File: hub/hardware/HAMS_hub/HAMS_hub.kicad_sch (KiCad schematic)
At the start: 32 parts, among them J1 Conn_02x07_Odd_Even, J10 Conn_01x04, J2 Conn_02x07_Odd_Even, J3 Conn_01x02, J4 Conn_01x04, J5 Conn_01x04, J6 Conn_01x07, J7 Conn_01x04, J8 Conn_01x04, J9 Conn_01x04, Q1 DMG3406L, U1 TCA9406DC, U2 NCP5501, U3 NRF24L01_Breakout

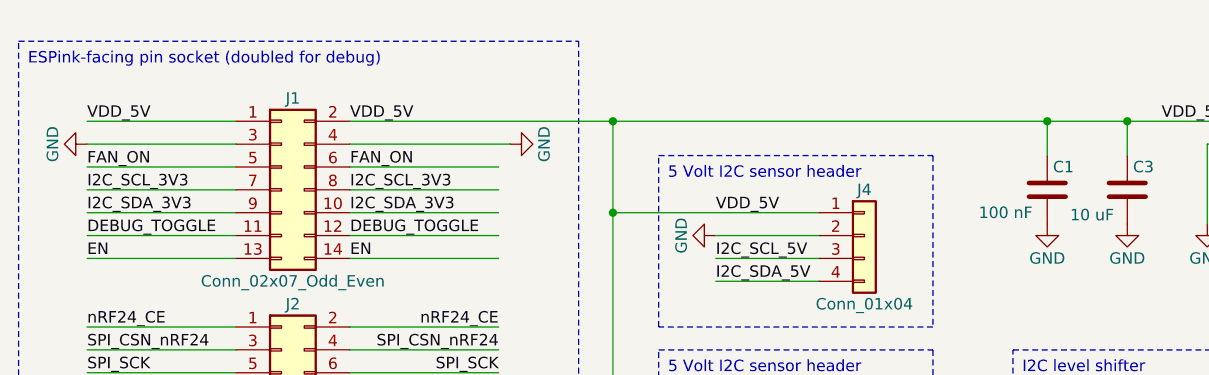
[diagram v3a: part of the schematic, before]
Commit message: Improve HAMS node & hub HW: PCB update
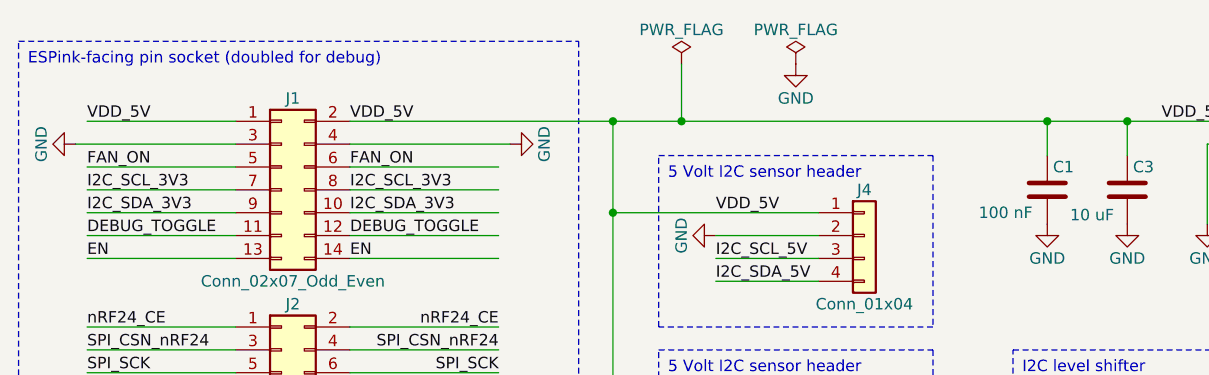
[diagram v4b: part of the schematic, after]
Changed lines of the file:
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@@
 	)
 	(junction
+		(at 90.17 25.4)
+		(diameter 0)
+		(color 0 0 0 0)
+	)
+	(junction
 		(at 233.68 118.11)
 		(diameter 0)
@@
 	(wire
 		(pts
-			(xy 82.55 25.4) (xy 130.81 25.4)
+			(xy 82.55 25.4) (xy 90.17 25.4)
 		)
 		(stroke
@@
 	(wire
 		(pts
-			(xy 24.13 27.94) (xy 40.64 27.94)
+			(xy 22.86 27.94) (xy 40.64 27.94)
 		)
 		(stroke
@@
 	(wire
 		(pts
+			(xy 90.17 25.4) (xy 130.81 25.4)
+		)
+		(stroke
+			(width 0)
+			(type default)
+		)
+	)
+	(wire
+		(pts
 			(xy 93.98 38.1) (xy 105.41 38.1)
 		)
@@
 	(wire
 		(pts
+			(xy 90.17 19.05) (xy 90.17 25.4)
+		)
+		(stroke
+			(width 0)
+			(type default)
+		)
+	)
+	(wire
+		(pts
 			(xy 24.13 48.26) (xy 40.64 48.26)
 		)
@@
 	)
 	(symbol
+		(lib_id "power:PWR_FLAG")
+		(at 102.87 19.05 0)
+		(unit 1)
+		(exclude_from_sim no)
+		(in_bom yes)
+		(on_board yes)
+		(dnp no)
+		(property "Reference" "#FLG02"
+			(at 102.87 17.145 0)
+			(effects
+				(font
+					(size 1.27 1.27)
+				)
+				(hide yes)
+			)
+		)
+		(property "Value" "PWR_FLAG"
+			(at 102.87 15.24 0)
+			(effects
+				(font
+					(size 1.27 1.27)
+				)
+			)
+		)
+		(property "Footprint" ""
+			(at 102.87 19.05 0)
+			(effects
+				(font
+					(size 1.27 1.27)
+				)
+				(hide yes)
+			)
+		)
+		(property "Datasheet" "~"
+			(at 102.87 19.05 0)
+			(effects
+				(font
+					(size 1.27 1.27)
+				)
+				(hide yes)
+			)
+		)
+		(property "Description" "Special symbol for telling ERC where power comes from"
+			(at 102.87 19.05 0)
+			(effects
+				(font
+					(size 1.27 1.27)
+				)
+				(hide yes)
+			)
+		)
+		(pin "1"
+		)
+		(instances
+			(project "HAMS_hub"
+				(path "/fa0fd52b-f5da-4d11-b769-e40ce6054164"
+					(reference "#FLG02")
+					(unit 1)
+				)
+			)
+		)
+	)
+	(symbol
 		(lib_id "power:GND")
 		(at 175.26 146.05 0)
@@
 	(symbol
 		(lib_id "power:GND")
-		(at 24.13 27.94 270)
+		(at 22.86 27.94 270)
 		(unit 1)
 		(exclude_from_sim no)
@@
 		(dnp no)
 		(property "Reference" "#PWR01"
-			(at 17.78 27.94 0)
+			(at 16.51 27.94 0)
 			(effects
 				(font
@@
 		)
 		(property "Value" "GND"
-			(at 20.32 27.94 0)
+			(at 19.05 27.94 0)
 			(effects
 				(font
@@
 		)
 		(property "Footprint" ""
-			(at 24.13 27.94 0)
+			(at 22.86 27.94 0)
 			(effects
 				(font
@@
 		)
 		(property "Datasheet" ""
-			(at 24.13 27.94 0)
+			(at 22.86 27.94 0)
 			(effects
 				(font
@@
 		)
 		(property "Description" "Power symbol creates a global label with name \"GND\" , ground"
-			(at 24.13 27.94 0)
+			(at 22.86 27.94 0)
 			(effects
 				(font
@@
 	(symbol
 		(lib_id "power:GND")
+		(at 102.87 19.05 0)
+		(unit 1)
+		(exclude_from_sim no)
+		(in_bom yes)
+		(on_board yes)
+		(dnp no)
+		(property "Reference" "#PWR029"
+			(at 102.87 25.4 0)
+			(effects
+				(font
+					(size 1.27 1.27)
+				)
+				(hide yes)
+			)
+		)
+		(property "Value" "GND"
+			(at 102.87 22.86 0)
+			(effects
+				(font
+					(size 1.27 1.27)
+				)
+			)
+		)
+		(property "Footprint" ""
+			(at 102.87 19.05 0)
+			(effects
+				(font
+					(size 1.27 1.27)
+				)
+				(hide yes)
+			)
+		)
+		(property "Datasheet" ""
+			(at 102.87 19.05 0)
+			(effects
+				(font
+					(size 1.27 1.27)
+				)
+				(hide yes)
+			)
+		)
+		(property "Description" "Power symbol creates a global label with name \"GND\" , ground"
+			(at 102.87 19.05 0)
+			(effects
+				(font
+					(size 1.27 1.27)
+				)
+				(hide yes)
+			)
+		)
+		(pin "1"
+		)
+		(instances
+			(project "HAMS_hub"
+				(path "/fa0fd52b-f5da-4d11-b769-e40ce6054164"
+					(reference "#PWR029")
+					(unit 1)
+				)
+			)
+		)
+	)
+	(symbol
+		(lib_id "power:GND")
 		(at 24.13 63.5 270)
 		(unit 1)
@@
 					(unit 1)
 				)
+			)
+		)
+	)
+	(symbol
+		(lib_id "power:PWR_FLAG")
+		(at 90.17 19.05 0)
+		(unit 1)
+		(exclude_from_sim no)
+		(in_bom yes)
+		(on_board yes)
+		(dnp no)
+		(property "Reference" "#FLG01"
+			(at 90.17 17.145 0)
+			(effects
+				(font
+					(size 1.27 1.27)
+				)
+				(hide yes)
+			)
+		)
+		(property "Value" "PWR_FLAG"
+			(at 90.17 15.24 0)
+			(effects
+				(font
+					(size 1.27 1.27)
+				)
+			)
+		)
+		(property "Footprint" ""
+			(at 90.17 19.05 0)
+			(effects
+				(font
+					(size 1.27 1.27)
+				)
+				(hide yes)
+			)
+		)
+		(property "Datasheet" "~"
+			(at 90.17 19.05 0)
+			(effects
+				(font
+					(size 1.27 1.27)
+				)
+				(hide yes)
+			)
+		)
+		(property "Description" "Special symbol for telling ERC where power comes from"
+			(at 90.17 19.05 0)
+			(effects
+				(font
+					(size 1.27 1.27)
+				)
+				(hide yes)
+			)
+		)
+		(pin "1"
+		)
+		(instances
+			(project ""
+				(path "/fa0fd52b-f5da-4d11-b769-e40ce6054164"
+					(reference "#FLG01")
+					(unit 1)
+				)

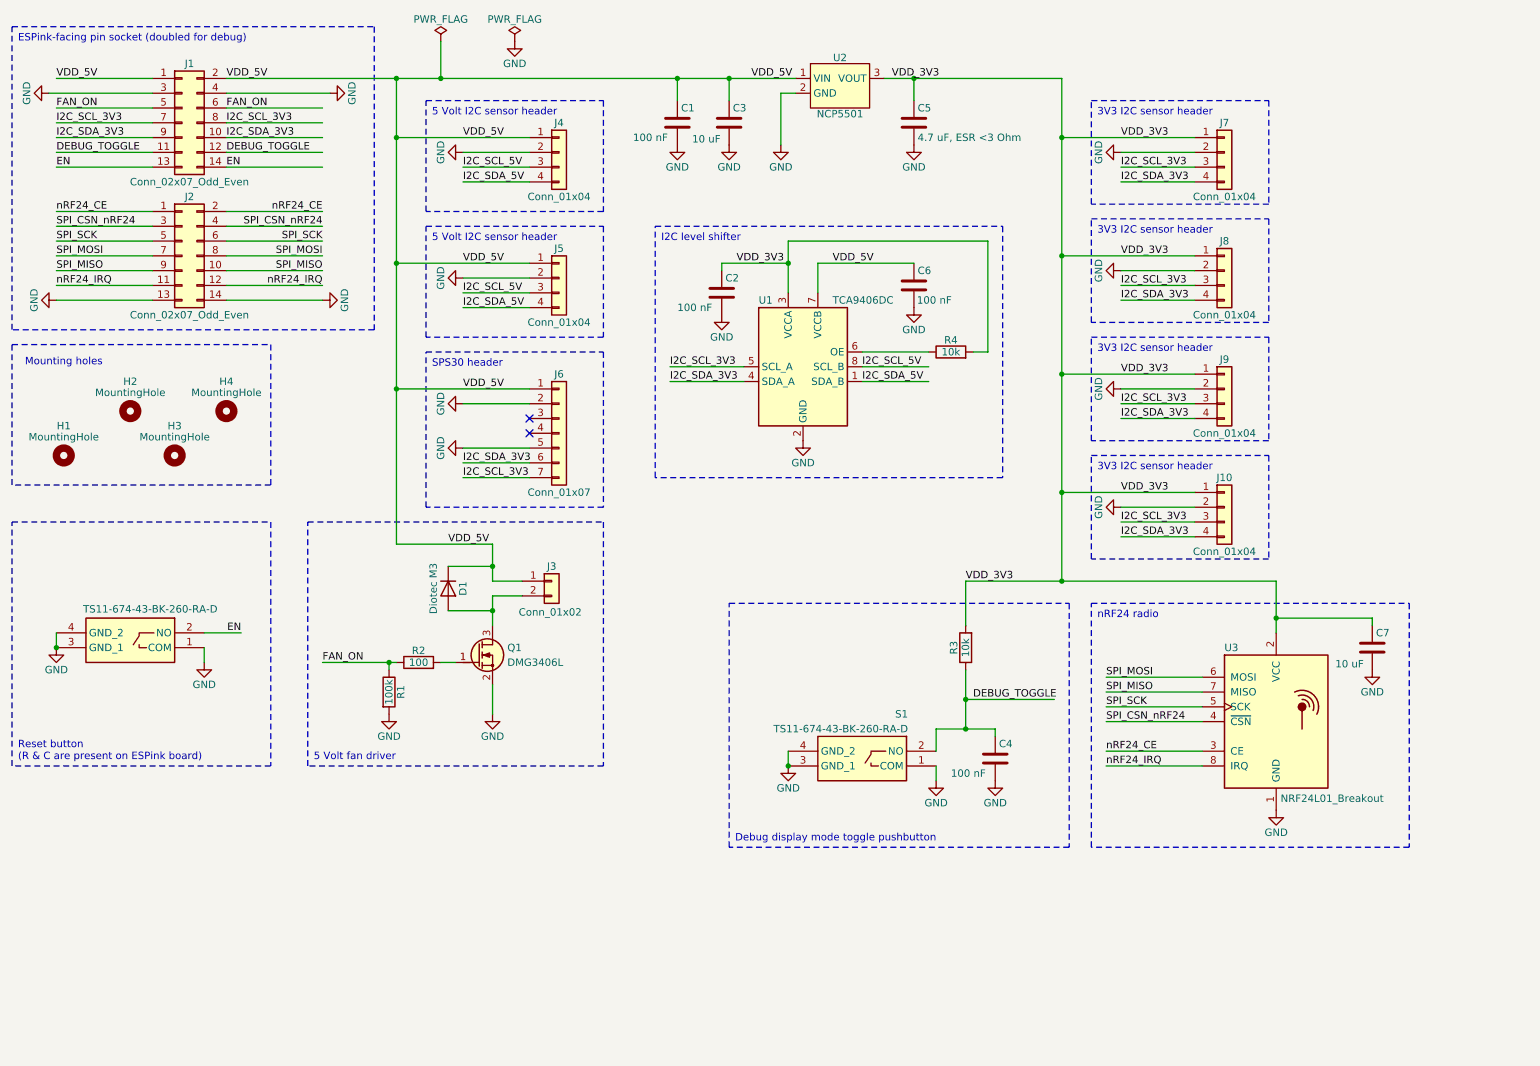
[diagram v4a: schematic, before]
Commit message: Update KiCAD files to version 9
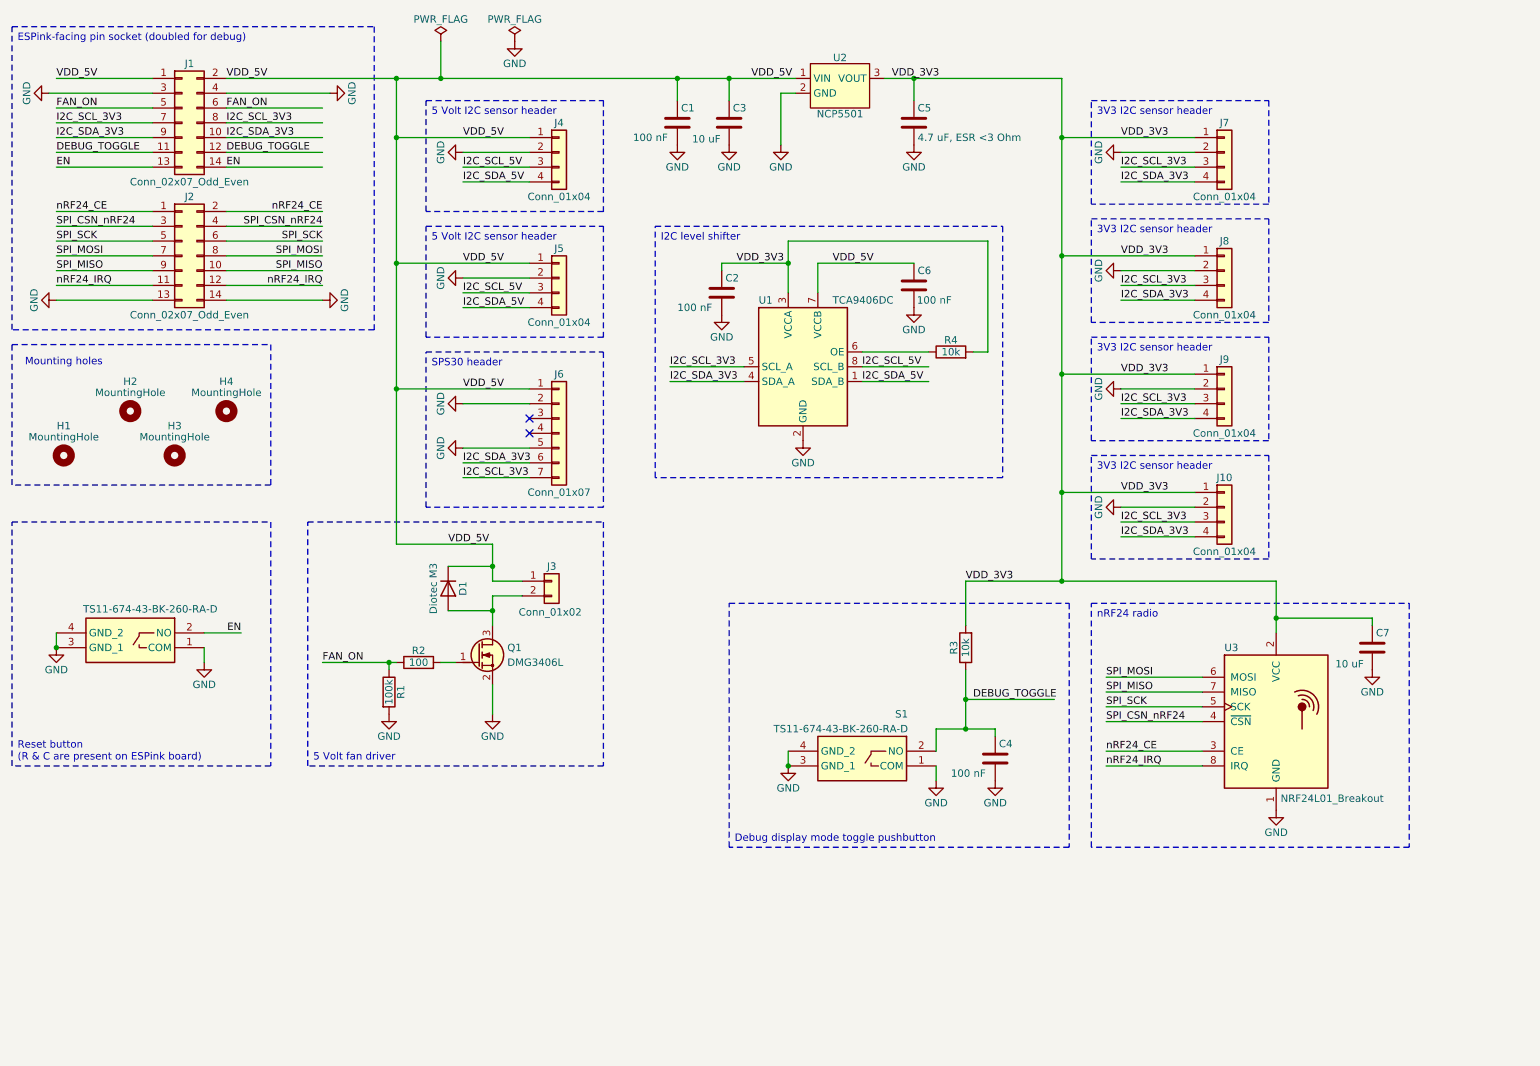
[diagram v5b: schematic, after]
